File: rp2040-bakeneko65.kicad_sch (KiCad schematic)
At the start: 31 parts, among them J1 SM04B-SRSS-TB, J2 SWD, SW85 SW_Push, U1 RP2040, U2 W25Q128JVS, U3 XC6206PxxxMR, U4 SRV05-4, Y1 12MHz

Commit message: (poorly) route JST
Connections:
- net D+: no longer R1.1
- net D-: now also U4.6 (IO4); no longer R2.1, U4.3 (IO2)
- net D_N: now also R2.1, U4.4 (IO3)
- net D_P: now also R1.1, U4.3 (IO2)
- no-connect marks 3 -> 1
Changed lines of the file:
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@@
   )
   (no_connect (at 262.89 24.765))
-  (no_connect (at 213.36 92.71))
-  (no_connect (at 187.96 92.71))
   (wire (pts (xy 74.93 21.59) (xy 77.47 21.59))
     (stroke (width 0) (type default))
@@
     (effects (font (size 1 1)) (justify left bottom))
   )
+  (label "D_N" (at 213.36 92.71 0) (fields_autoplaced)
+    (effects (font (size 1.27 1.27)) (justify left bottom))
+  )
+  (label "D_P" (at 33.02 36.83 180) (fields_autoplaced)
+    (effects (font (size 1.27 1.27)) (justify right bottom))
+  )
+  (label "D_P" (at 213.36 87.63 0) (fields_autoplaced)
+    (effects (font (size 1.27 1.27)) (justify left bottom))
+  )
+  (label "D_N" (at 33.02 39.37 180) (fields_autoplaced)
+    (effects (font (size 1.27 1.27)) (justify right bottom))
+  )
   (global_label "XTAL_OUT" (shape input) (at 44.45 85.09 180) (fields_autoplaced)
     (effects (font (size 1.27 1.27)) (justify right))
@@
     )
   )
-  (global_label "D-" (shape input) (at 33.02 39.37 180) (fields_autoplaced)
-    (effects (font (size 1.27 1.27)) (justify right))
-    (property "Intersheetrefs" "${INTERSHEET_REFS}" (at 27.7645 39.2906 0)
-      (effects (font (size 1.27 1.27)) (justify right) hide)
-    )
-  )
   (global_label "SD1" (shape input) (at 153.67 30.48 0) (fields_autoplaced)
     (effects (font (size 1.27 1.27)) (justify left))
@@
     )
   )
-  (global_label "D-" (shape input) (at 213.36 87.63 0) (fields_autoplaced)
-    (effects (font (size 1.27 1.27)) (justify left))
-    (property "Intersheetrefs" "${INTERSHEET_REFS}" (at 218.6155 87.5506 0)
-      (effects (font (size 1.27 1.27)) (justify left) hide)
+  (global_label "D-" (shape input) (at 187.96 92.71 180) (fields_autoplaced)
+    (effects (font (size 1.27 1.27)) (justify right))
+    (property "Intersheetrefs" "${INTERSHEET_REFS}" (at 182.2118 92.71 0)
+      (effects (font (size 1.27 1.27)) (justify right) hide)
     )
   )
@@
   (global_label "D+" (shape input) (at 187.96 87.63 180) (fields_autoplaced)
     (effects (font (size 1.27 1.27)) (justify right))
-    (property "Intersheetrefs" "${INTERSHEET_REFS}" (at 182.7045 87.5506 0)
+    (property "Intersheetrefs" "${INTERSHEET_REFS}" (at 182.2118 87.63 0)
       (effects (font (size 1.27 1.27)) (justify right) hide)
     )
@@
       (effects (font (size 1.27 1.27)) (justify right) hide)
     )
-  )
-  (global_label "D+" (shape input) (at 33.02 36.83 180) (fields_autoplaced)
-    (effects (font (size 1.27 1.27)) (justify right))
-    (property "Intersheetrefs" "${INTERSHEET_REFS}" (at 27.7645 36.7506 0)
-      (effects (font (size 1.27 1.27)) (justify right) hide)
-    )

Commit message: flash, redo ESD, some other stuff
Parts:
- U4: value SRV05-4 -> SRV05
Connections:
- net D+: now also R1.1
- net D-: now also R2.1
- net D_N: no longer R2.1, U4.4 (IO3)
- net D_P: no longer R1.1, U4.3 (IO2)
- no-connect marks 1 -> 3
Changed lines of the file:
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@@
   )
   (no_connect (at 262.89 24.765))
+  (no_connect (at 213.36 87.63))
+  (no_connect (at 213.36 92.71))
   (wire (pts (xy 74.93 21.59) (xy 77.47 21.59))
     (stroke (width 0) (type default))
@@
   (label "D_N" (at 44.45 39.37 0) (fields_autoplaced)
     (effects (font (size 1 1)) (justify left bottom))
-  )
-  (label "D_N" (at 213.36 92.71 0) (fields_autoplaced)
-    (effects (font (size 1.27 1.27)) (justify left bottom))
-  )
-  (label "D_P" (at 33.02 36.83 180) (fields_autoplaced)
-    (effects (font (size 1.27 1.27)) (justify right bottom))
-  )
-  (label "D_P" (at 213.36 87.63 0) (fields_autoplaced)
-    (effects (font (size 1.27 1.27)) (justify left bottom))
-  )
-  (label "D_N" (at 33.02 39.37 180) (fields_autoplaced)
-    (effects (font (size 1.27 1.27)) (justify right bottom))
   )
   (global_label "XTAL_OUT" (shape input) (at 44.45 85.09 180) (fields_autoplaced)
@@
     )
   )
+  (global_label "D+" (shape input) (at 33.02 36.83 180) (fields_autoplaced)
+    (effects (font (size 1.27 1.27)) (justify right))
+    (property "Intersheetrefs" "${INTERSHEET_REFS}" (at 27.2718 36.83 0)
+      (effects (font (size 1.27 1.27)) (justify right) hide)
+    )
+  )
   (global_label "CS" (shape input) (at 46.99 46.99 180) (fields_autoplaced)
     (effects (font (size 1.27 1.27)) (justify right))
@@
     )
   )
+  (global_label "D-" (shape input) (at 33.02 39.37 180) (fields_autoplaced)
+    (effects (font (size 1.27 1.27)) (justify right))
+    (property "Intersheetrefs" "${INTERSHEET_REFS}" (at 27.2718 39.37 0)
+      (effects (font (size 1.27 1.27)) (justify right) hide)
+    )
+  )
   (global_label "QSPI_CLK" (shape input) (at 128.27 35.56 180) (fields_autoplaced)
     (effects (font (size 1.27 1.27)) (justify right))
@@
   (symbol (lib_id "marbastlib-various:SRV05-4") (at 200.66 90.17 0) (unit 1)
     (in_bom yes) (on_board yes) (dnp no) (fields_autoplaced)
-    (property "Reference" "U4" (at 203.4287 74.93 0)
+    (property "Reference" "U4" (at 203.8097 76.2 0)
       (effects (font (size 1.27 1.27)) (justify left))
     )
-    (property "Value" "SRV05-4" (at 203.4287 77.47 0)
+    (property "Value" "SRV05" (at 203.8097 78.74 0)
       (effects (font (size 1.27 1.27)) (justify left))
     )

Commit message: USB boot
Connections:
- net +3V3: no longer R3.1
- net CS: now also R3.2
- net RESET: no longer R3.2, SW85.2
- new net: R3.1, SW85.2
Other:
- moved on the sheet: C1, R3, SW85, U2

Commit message: LED + decoupling caps + a lot of stuff
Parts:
- added C18: 100nF, Capacitor_SMD:C_0402_1005Metric, symbol Device:C_Small
- added R5: 1k, Resistor_SMD:R_0402_1005Metric, symbol Device:R_Small
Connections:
- net +3V3: now also R5.2
- net +5V: now also C18.1; no longer LED1.1 (VDD)
- net RESET: now also R5.1
- new net: C18.2, LED1.1 (VDD)
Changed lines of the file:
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@@
   (junction (at 201.93 48.26) (diameter 0) (color 0 0 0 0)
+  )
+  (junction (at 43.18 29.21) (diameter 0) (color 0 0 0 0)
   )
   (junction (at 236.22 48.26) (diameter 0) (color 0 0 0 0)
@@
     (stroke (width 0) (type solid))
   )
+  (wire (pts (xy 43.18 18.796) (xy 43.18 21.082))
+    (stroke (width 0) (type default))
+  )
+  (wire (pts (xy 43.18 26.162) (xy 43.18 29.21))
+    (stroke (width 0) (type default))
+  )
   (wire (pts (xy 224.79 55.88) (xy 236.22 55.88))
     (stroke (width 0) (type default))
@@
     (stroke (width 0) (type default))
   )
+  (wire (pts (xy 39.37 29.21) (xy 43.18 29.21))
+    (stroke (width 0) (type default))
+  )
   (wire (pts (xy 121.285 69.215) (xy 121.285 71.755))
     (stroke (width 0) (type default))
@@
     (stroke (width 0) (type default))
   )
+  (wire (pts (xy 245.11 17.145) (xy 247.65 17.145))
+    (stroke (width 0) (type default))
+  )
   (wire (pts (xy 123.19 30.48) (xy 124.46 30.48))
     (stroke (width 0) (type default))
@@
     (stroke (width 0) (type default))
   )
+  (wire (pts (xy 43.18 29.21) (xy 46.99 29.21))
+    (stroke (width 0) (type default))
+  )
   (wire (pts (xy 137.16 64.135) (xy 153.035 64.135))
     (stroke (width 0) (type default))
@@
   )
   (wire (pts (xy 139.7 22.86) (xy 144.145 22.86))
+    (stroke (width 0) (type default))
+  )
+  (wire (pts (xy 252.73 17.145) (xy 255.27 17.145))
     (stroke (width 0) (type default))
   )
@@
     )
   )
-  (global_label "RESET" (shape input) (at 46.99 29.21 180) (fields_autoplaced)
-    (effects (font (size 1.27 1.27)) (justify right))
-    (property "Intersheetrefs" "${INTERSHEET_REFS}" (at 38.3391 29.21 0)
+  (global_label "RESET" (shape input) (at 39.37 29.21 180) (fields_autoplaced)
+    (effects (font (size 1.27 1.27)) (justify right))
+    (property "Intersheetrefs" "${INTERSHEET_REFS}" (at 30.7191 29.21 0)
       (effects (font (size 1.27 1.27)) (justify right) hide)
     )
@@
     )
   )
+  (symbol (lib_id "Device:C_Small") (at 250.19 17.145 90) (unit 1)
+    (in_bom yes) (on_board yes) (dnp no)
+    (property "Reference" "C18" (at 248.285 13.97 90)
+      (effects (font (size 1.27 1.27)))
+    )
+    (property "Value" "100nF" (at 254.635 13.97 90)
+      (effects (font (size 1.27 1.27)))
+    )
+    (property "Footprint" "Capacitor_SMD:C_0402_1005Metric" (at 250.19 17.145 0)
+      (effects (font (size 1.27 1.27)) hide)
+    )
+    (property "Datasheet" "~" (at 250.19 17.145 0)
+      (effects (font (size 1.27 1.27)) hide)
+    )
+    (pin "1")
+    (pin "2")
+    (instances
+      (project "rp2040-bakeneko65"
+        (path "/6136f036-b0e3-42a2-8ab6-1b828fccf946"
+          (reference "C18") (unit 1)
+        )
+      )
+    )
+  )
   (symbol (lib_id "Device:C_Small") (at 201.93 50.8 0) (unit 1)
     (in_bom yes) (on_board yes) (dnp no)
@@
         (path "/6136f036-b0e3-42a2-8ab6-1b828fccf946"
           (reference "R3") (unit 1)
+        )
+      )
+    )
+  )
+  (symbol (lib_id "Device:R_Small") (at 43.18 23.622 180) (unit 1)
+    (in_bom yes) (on_board yes) (dnp no) (fields_autoplaced)
+    (property "Reference" "R5" (at 45.72 22.987 0)
+      (effects (font (size 1.27 1.27)) (justify right))
+    )
+    (property "Value" "1k" (at 45.72 25.527 0)
+      (effects (font (size 1.27 1.27)) (justify right))
+    )
+    (property "Footprint" "Resistor_SMD:R_0402_1005Metric" (at 43.18 23.622 0)
+      (effects (font (size 1.27 1.27)) hide)
+    )
+    (property "Datasheet" "~" (at 43.18 23.622 0)
+      (effects (font (size 1.27 1.27)) hide)
+    )
+    (pin "1")
+    (pin "2")
+    (instances
+      (project "rp2040-bakeneko65"
+        (path "/6136f036-b0e3-42a2-8ab6-1b828fccf946"
+          (reference "R5") (unit 1)
         )
       )
@@
         (path "/6136f036-b0e3-42a2-8ab6-1b828fccf946"
           (reference "#PWR0119") (unit 1)
+        )
+      )
+    )
+  )
+  (symbol (lib_name "+3V3_1") (lib_id "power:+3V3") (at 43.18 18.796 0) (unit 1)
+    (in_bom yes) (on_board yes) (dnp no) (fields_autoplaced)
+    (property "Reference" "#PWR066" (at 43.18 22.606 0)
+      (effects (font (size 1.27 1.27)) hide)
+    )
+    (property "Value" "+3V3" (at 43.18 15.24 0)
+      (effects (font (size 1.27 1.27)))
+    )
+    (property "Footprint" "" (at 43.18 18.796 0)
+      (effects (font (size 1.27 1.27)) hide)
+    )
+    (property "Datasheet" "" (at 43.18 18.796 0)
+      (effects (font (size 1.27 1.27)) hide)
+    )
+    (pin "1")
+    (instances
+      (project "rp2040-bakeneko65"
+        (path "/6136f036-b0e3-42a2-8ab6-1b828fccf946"
+          (reference "#PWR066") (unit 1)
         )
       )
@@
     )
   )
-  (symbol (lib_id "power:+5V") (at 255.27 17.145 0) (unit 1)
-    (in_bom yes) (on_board yes) (dnp no)
-    (property "Reference" "#PWR0124" (at 255.27 20.955 0)
-      (effects (font (size 1.27 1.27)) hide)
-    )
-    (property "Value" "+5V" (at 257.175 17.145 0)
-      (effects (font (size 1.27 1.27)))
-    )
-    (property "Footprint" "" (at 255.27 17.145 0)
-      (effects (font (size 1.27 1.27)) hide)
-    )
-    (property "Datasheet" "" (at 255.27 17.145 0)
-      (effects (font (size 1.27 1.27)) hide)
-    )
+  (symbol (lib_id "power:+5V") (at 245.11 17.145 0) (unit 1)
+    (in_bom yes) (on_board yes) (dnp no)
+    (property "Reference" "#PWR0124" (at 245.11 20.955 0)
+      (effects (font (size 1.27 1.27)) hide)
+    )
+    (property "Value" "+5V" (at 241.935 17.145 0)
+      (effects (font (size 1.27 1.27)))
+    )
+    (property "Footprint" "" (at 245.11 17.145 0)
+      (effects (font (size 1.27 1.27)) hide)
+    )
+    (property "Datasheet" "" (at 245.11 17.145 0)
+      (effects (font (size 1.27 1.27)) hide)
+    )

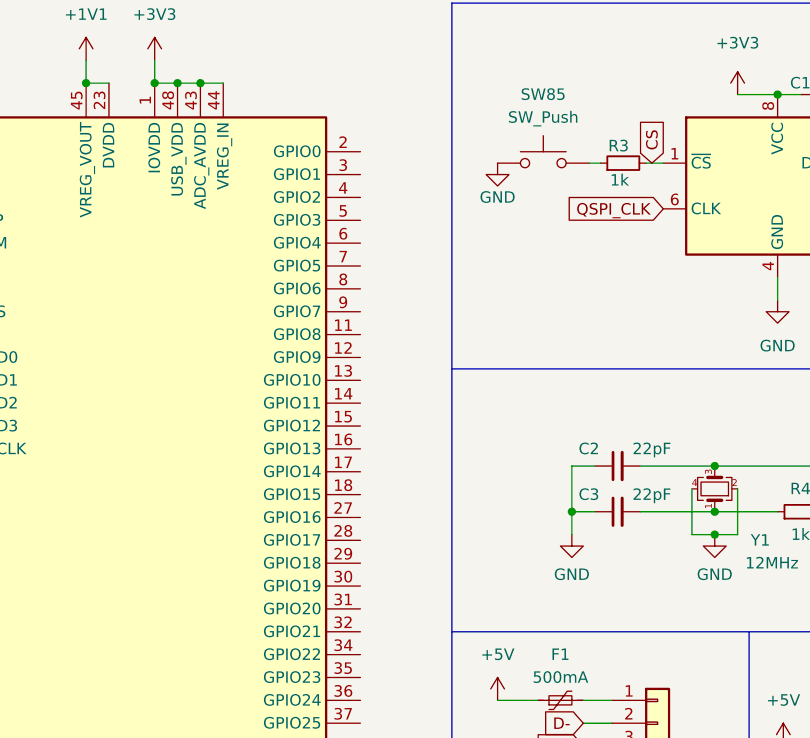
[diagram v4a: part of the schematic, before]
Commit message: column routing
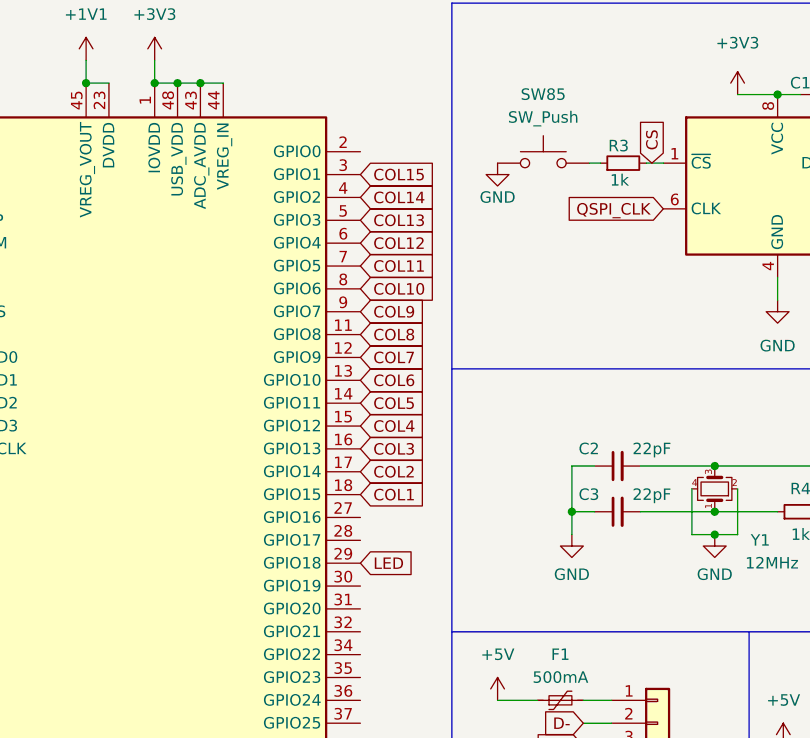
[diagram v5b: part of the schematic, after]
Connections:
- net LED: now also U1.29 (GPIO18)
- net COL8: now reaches U1.11 (GPIO8)
- net COL7: now reaches U1.12 (GPIO9)
- net COL6: now reaches U1.13 (GPIO10)
- net COL5: now reaches U1.14 (GPIO11)
- net COL4: now reaches U1.15 (GPIO12)
- net COL3: now reaches U1.16 (GPIO13)
- net COL2: now reaches U1.17 (GPIO14)
- net COL1: now reaches U1.18 (GPIO15)
- net COL15: now reaches U1.3 (GPIO1)
- net COL14: now reaches U1.4 (GPIO2)
- net COL13: now reaches U1.5 (GPIO3)
- net COL12: now reaches U1.6 (GPIO4)
- net COL11: now reaches U1.7 (GPIO5)
- net COL10: now reaches U1.8 (GPIO6)
- net COL9: now reaches U1.9 (GPIO7)
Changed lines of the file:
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@@
+    )
+  )
+  (global_label "COL11" (shape input) (at 97.79 41.91 0) (fields_autoplaced)
+    (effects (font (size 1.27 1.27)) (justify left))
+    (property "Intersheetrefs" "${INTERSHEET_REFS}" (at 106.7434 41.91 0)
+      (effects (font (size 1.27 1.27)) (justify left) hide)
     )
   )
@@
     )
   )
+  (global_label "COL9" (shape input) (at 97.79 46.99 0) (fields_autoplaced)
+    (effects (font (size 1.27 1.27)) (justify left))
+    (property "Intersheetrefs" "${INTERSHEET_REFS}" (at 105.5339 46.99 0)
+      (effects (font (size 1.27 1.27)) (justify left) hide)
+    )
+  )
   (global_label "XTAL_IN" (shape input) (at 44.45 74.93 180) (fields_autoplaced)
     (effects (font (size 1.27 1.27)) (justify right))
@@
     )
   )
+  (global_label "LED" (shape input) (at 97.79 74.93 0) (fields_autoplaced)
+    (effects (font (size 1.27 1.27)) (justify left))
+    (property "Intersheetrefs" "${INTERSHEET_REFS}" (at 104.1429 74.93 0)
+      (effects (font (size 1.27 1.27)) (justify left) hide)
+    )
+  )
   (global_label "CS" (shape input) (at 46.99 46.99 180) (fields_autoplaced)
     (effects (font (size 1.27 1.27)) (justify right))
@@
     )
   )
+  (global_label "COL7" (shape input) (at 97.79 52.07 0) (fields_autoplaced)
+    (effects (font (size 1.27 1.27)) (justify left))
+    (property "Intersheetrefs" "${INTERSHEET_REFS}" (at 105.5339 52.07 0)
+      (effects (font (size 1.27 1.27)) (justify left) hide)
+    )
+  )
   (global_label "QSPI_CLK" (shape input) (at 46.99 62.23 180) (fields_autoplaced)
     (effects (font (size 1.27 1.27)) (justify right))
@@
     )
   )
+  (global_label "COL13" (shape input) (at 97.79 36.83 0) (fields_autoplaced)
+    (effects (font (size 1.27 1.27)) (justify left))
+    (property "Intersheetrefs" "${INTERSHEET_REFS}" (at 106.7434 36.83 0)
+      (effects (font (size 1.27 1.27)) (justify left) hide)
+    )
+  )
   (global_label "RESET" (shape input) (at 39.37 29.21 180) (fields_autoplaced)
     (effects (font (size 1.27 1.27)) (justify right))
@@
     )
   )
+  (global_label "COL12" (shape input) (at 97.79 39.37 0) (fields_autoplaced)
+    (effects (font (size 1.27 1.27)) (justify left))
+    (property "Intersheetrefs" "${INTERSHEET_REFS}" (at 106.7434 39.37 0)
+      (effects (font (size 1.27 1.27)) (justify left) hide)
+    )
+  )
   (global_label "SWD" (shape input) (at 125.73 124.46 180) (fields_autoplaced)
     (effects (font (size 1.27 1.27)) (justify right))
@@
     )
   )
+  (global_label "COL5" (shape input) (at 97.79 57.15 0) (fields_autoplaced)
+    (effects (font (size 1.27 1.27)) (justify left))
+    (property "Intersheetrefs" "${INTERSHEET_REFS}" (at 105.5339 57.15 0)
+      (effects (font (size 1.27 1.27)) (justify left) hide)
+    )
+  )
+  (global_label "COL15" (shape input) (at 97.79 31.75 0) (fields_autoplaced)
+    (effects (font (size 1.27 1.27)) (justify left))
+    (property "Intersheetrefs" "${INTERSHEET_REFS}" (at 106.7434 31.75 0)
+      (effects (font (size 1.27 1.27)) (justify left) hide)
+    )
+  )
   (global_label "SD0" (shape input) (at 156.845 27.94 0) (fields_autoplaced)
     (effects (font (size 1.27 1.27)) (justify left))
@@
     )
   )
+  (global_label "COL1" (shape input) (at 97.79 67.31 0) (fields_autoplaced)
+    (effects (font (size 1.27 1.27)) (justify left))
+    (property "Intersheetrefs" "${INTERSHEET_REFS}" (at 105.5339 67.31 0)
+      (effects (font (size 1.27 1.27)) (justify left) hide)
+    )
+  )
   (global_label "SD1" (shape input) (at 46.99 54.61 180) (fields_autoplaced)
     (effects (font (size 1.27 1.27)) (justify right))
@@
     )
   )
+  (global_label "COL6" (shape input) (at 97.79 54.61 0) (fields_autoplaced)
+    (effects (font (size 1.27 1.27)) (justify left))
+    (property "Intersheetrefs" "${INTERSHEET_REFS}" (at 105.5339 54.61 0)
+      (effects (font (size 1.27 1.27)) (justify left) hide)
+    )
+  )
   (global_label "SD2" (shape input) (at 46.99 57.15 180) (fields_autoplaced)
     (effects (font (size 1.27 1.27)) (justify right))
@@
     )
   )
+  (global_label "COL14" (shape input) (at 97.79 34.29 0) (fields_autoplaced)
+    (effects (font (size 1.27 1.27)) (justify left))
+    (property "Intersheetrefs" "${INTERSHEET_REFS}" (at 106.7434 34.29 0)
+      (effects (font (size 1.27 1.27)) (justify left) hide)
+    )
+  )
   (global_label "SWCLK" (shape input) (at 125.73 127 180) (fields_autoplaced)
     (effects (font (size 1.27 1.27)) (justify right))
@@
     )
   )
+  (global_label "COL3" (shape input) (at 97.79 62.23 0) (fields_autoplaced)
+    (effects (font (size 1.27 1.27)) (justify left))
+    (property "Intersheetrefs" "${INTERSHEET_REFS}" (at 105.5339 62.23 0)
+      (effects (font (size 1.27 1.27)) (justify left) hide)
+    )
+  )
   (global_label "SD0" (shape input) (at 46.99 52.07 180) (fields_autoplaced)
     (effects (font (size 1.27 1.27)) (justify right))
@@
     )
   )
+  (global_label "COL4" (shape input) (at 97.79 59.69 0) (fields_autoplaced)
+    (effects (font (size 1.27 1.27)) (justify left))
+    (property "Intersheetrefs" "${INTERSHEET_REFS}" (at 105.5339 59.69 0)
+      (effects (font (size 1.27 1.27)) (justify left) hide)
+    )
+  )
   (global_label "QSPI_CLK" (shape input) (at 131.445 35.56 180) (fields_autoplaced)
     (effects (font (size 1.27 1.27)) (justify right))
@@
     )
   )
+  (global_label "COL8" (shape input) (at 97.79 49.53 0) (fields_autoplaced)
+    (effects (font (size 1.27 1.27)) (justify left))
+    (property "Intersheetrefs" "${INTERSHEET_REFS}" (at 105.5339 49.53 0)
+      (effects (font (size 1.27 1.27)) (justify left) hide)
+    )
+  )
   (global_label "D+" (shape input) (at 122.555 95.25 180) (fields_autoplaced)
     (effects (font (size 1.27 1.27)) (justify right))
@@
     )
   )
+  (global_label "COL2" (shape input) (at 97.79 64.77 0) (fields_autoplaced)
+    (effects (font (size 1.27 1.27)) (justify left))
+    (property "Intersheetrefs" "${INTERSHEET_REFS}" (at 105.5339 64.77 0)
+      (effects (font (size 1.27 1.27)) (justify left) hide)
+    )
+  )
+  (global_label "COL10" (shape input) (at 97.79 44.45 0) (fields_autoplaced)
+    (effects (font (size 1.27 1.27)) (justify left))
+    (property "Intersheetrefs" "${INTERSHEET_REFS}" (at 106.7434 44.45 0)
+      (effects (font (size 1.27 1.27)) (justify left) hide)
+    )
+  )
